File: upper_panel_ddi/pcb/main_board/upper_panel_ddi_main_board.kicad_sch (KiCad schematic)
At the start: 9 parts, among them J1 ROW0, J2 ROW1, J3 ROW2, J4 ROW3, J5 ROW4, J6 ROW5, J7 ROW6, J8 ROW7

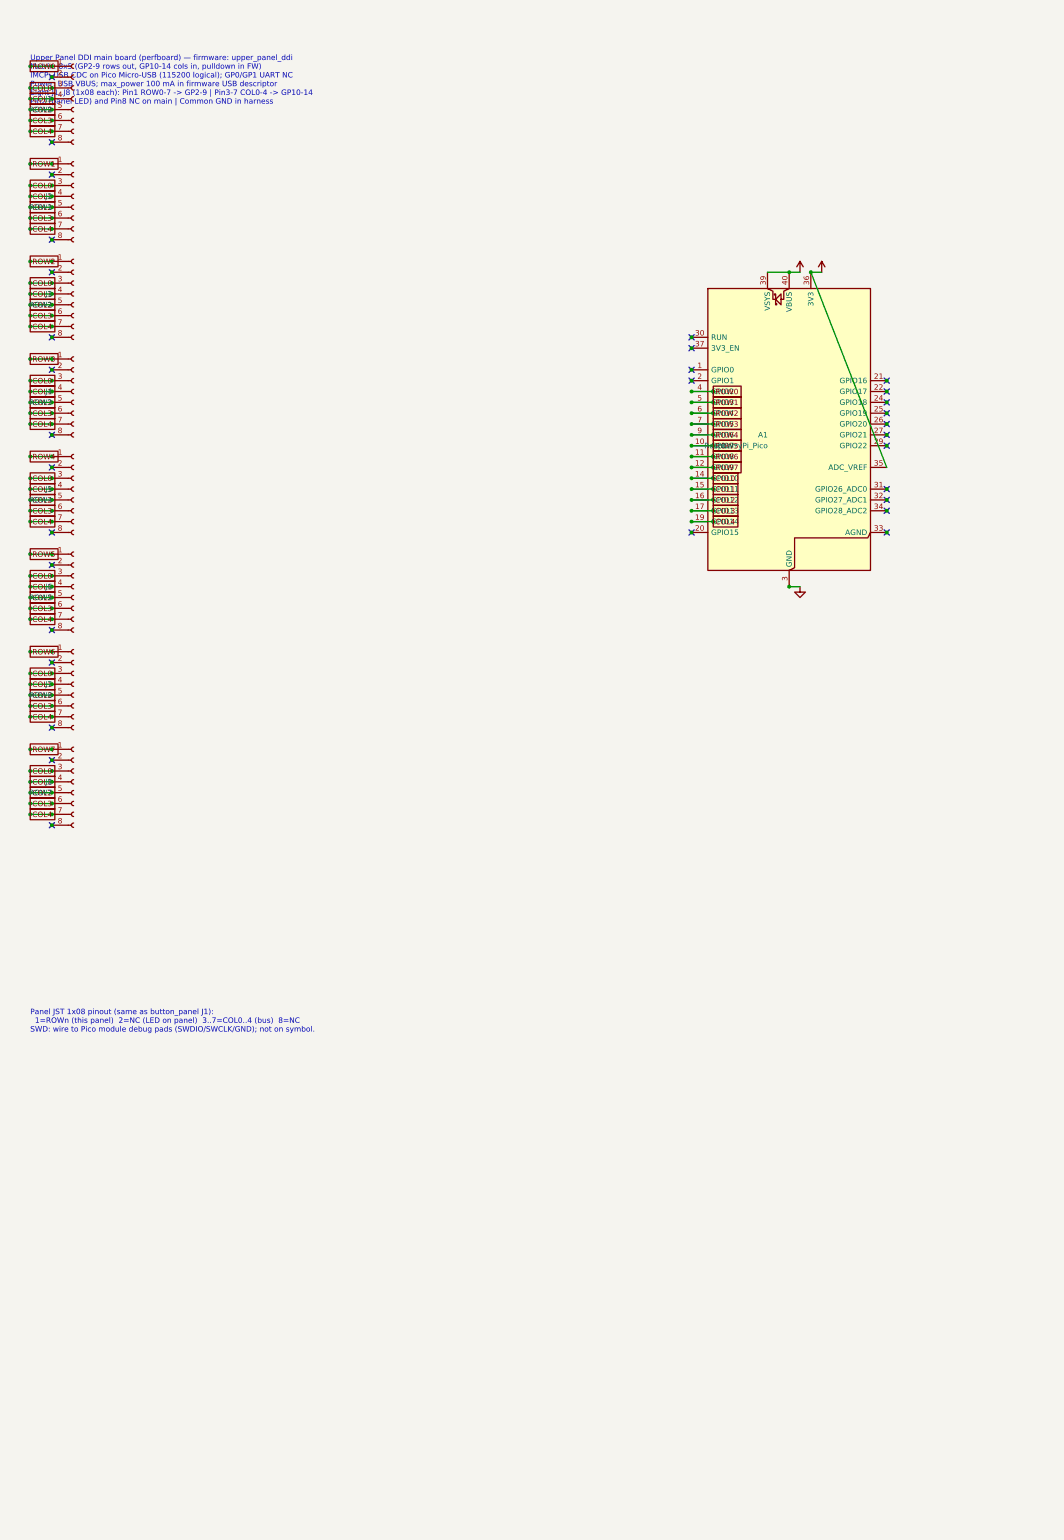
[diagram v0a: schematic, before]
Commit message: fix(hardware): wire main board without global labels
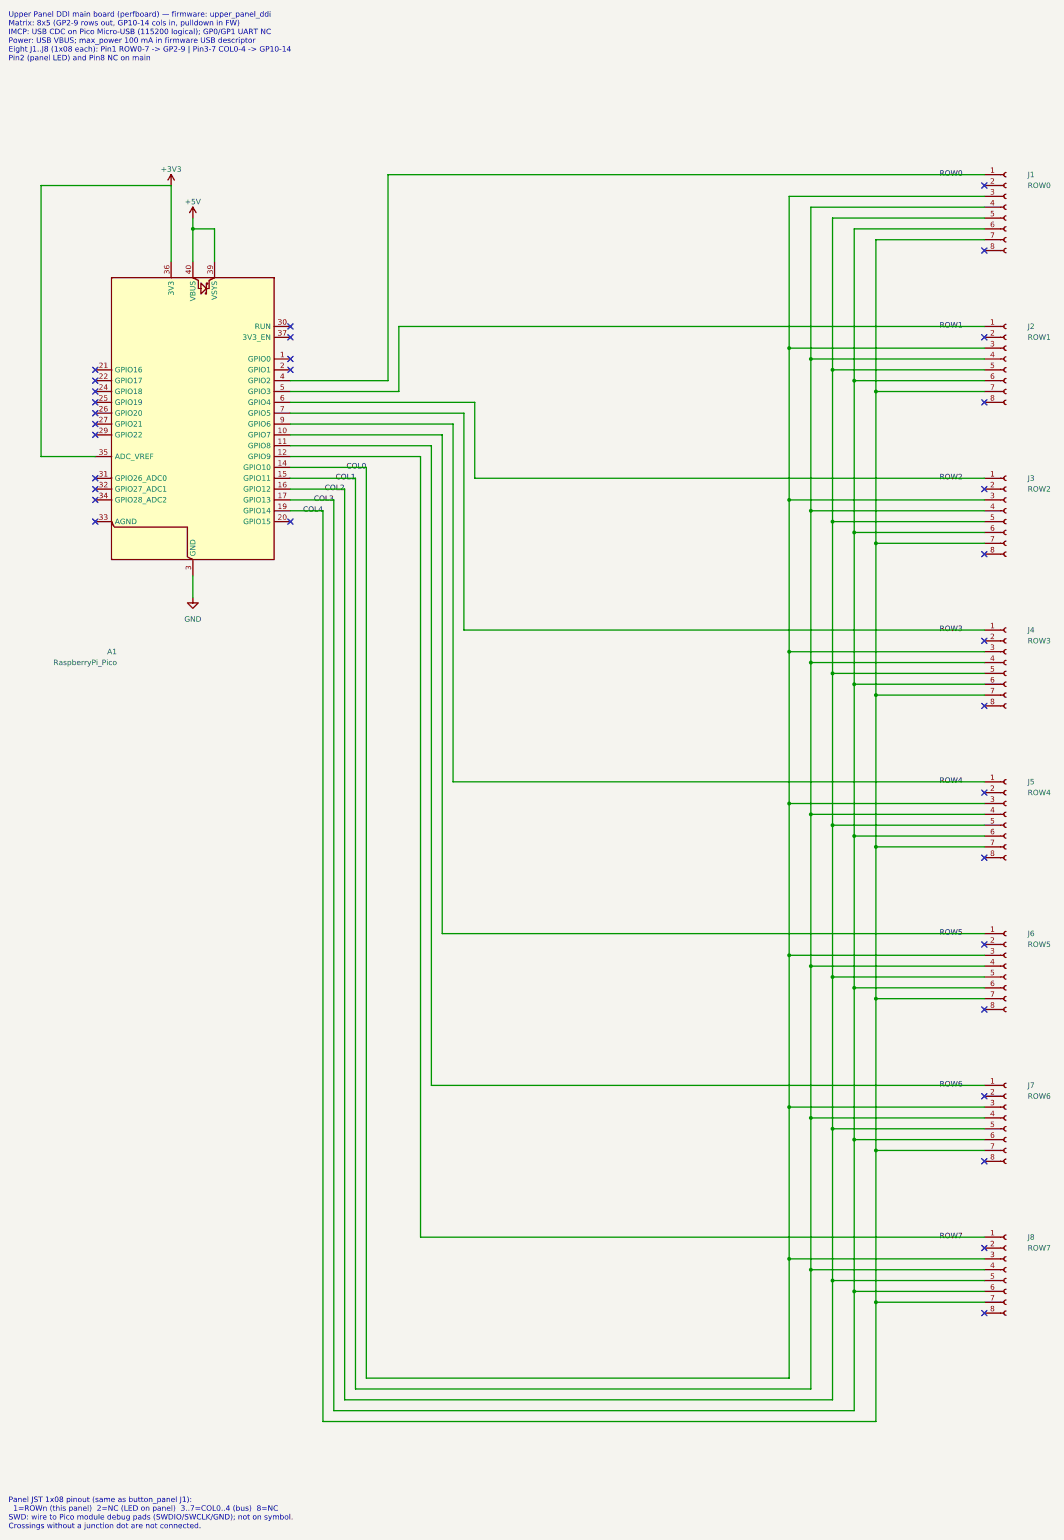
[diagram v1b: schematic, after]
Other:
- note added: "Panel JST 1x08 pinout (same as button_panel J1): 1=ROWn (this panel) 2=NC (LED on panel) 3..7=COL0..4 (bus) 8=NC SWD: wire to Pico module debug pads (SWDIO/SWCLK/GND); not on symbol. Crossings without a junction dot are not connected."
- note added: "Upper Panel DDI main board (perfboard) — firmware: upper_panel_ddi Matrix: 8x5 (GP2-9 rows out, GP10-14 cols in, pulldown in FW) IMCP: USB CDC on Pico Micro-USB (115200 logical); GP0/GP1 UART NC Power: USB VBUS; max_power 100 mA in firmware USB descriptor Eight J1..J8 (1x08 each): Pin1 ROW0-7 -> GP2-9 | Pin3-7 COL0-4 -> GP10-14 Pin2 (panel LED) and Pin8 NC on main"
- note removed: "Panel JST 1x08 pinout (same as button_panel J1): 1=ROWn (this panel) 2=NC (LED on panel) 3..7=COL0..4 (bus) 8=NC SWD: wire to Pico module debug pads (SWDIO/SWCLK/GND); not on symbol."
- note removed: "Upper Panel DDI main board (perfboard) — firmware: upper_panel_ddi Matrix: 8x5 (GP2-9 rows out, GP10-14 cols in, pulldown in FW) IMCP: USB CDC on Pico Micro-USB (115200 logical); GP0/GP1 UART NC Power: USB VBUS; max_power 100 mA in firmware USB descriptor Eight J1..J8 (1x08 each): Pin1 ROW0-7 -> GP2-9 | Pin3-7 COL0-4 -> GP10-14 Pin2 (panel LED) and Pin8 NC on main | Common GND in harness"
- moved on the sheet: A1
